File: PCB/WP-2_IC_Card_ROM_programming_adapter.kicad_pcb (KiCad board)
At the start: 2 copper layers, 17.8 x 49.5 mm, 3 parts, among them J1 Conn_01x38_Male, J2 Conn_02x16_Counter_Clockwise

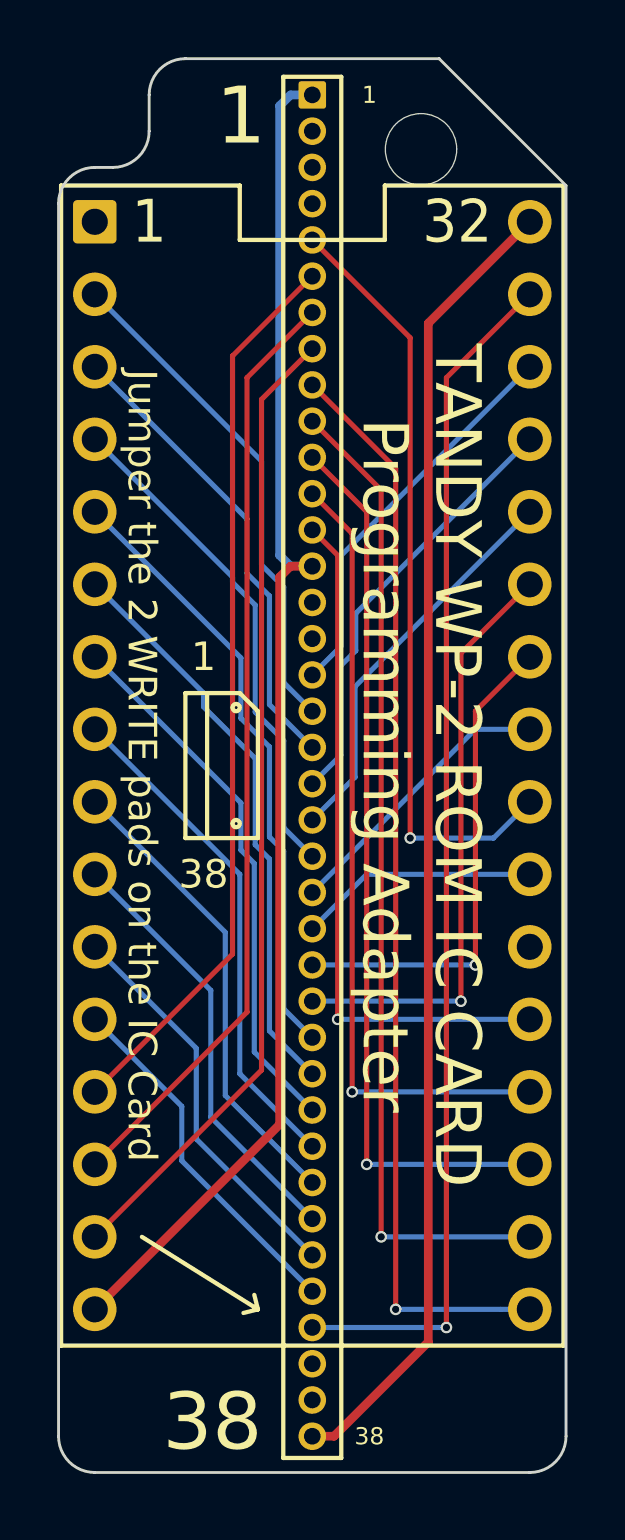
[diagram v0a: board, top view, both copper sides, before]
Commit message: fine-tune via-near-trace placements
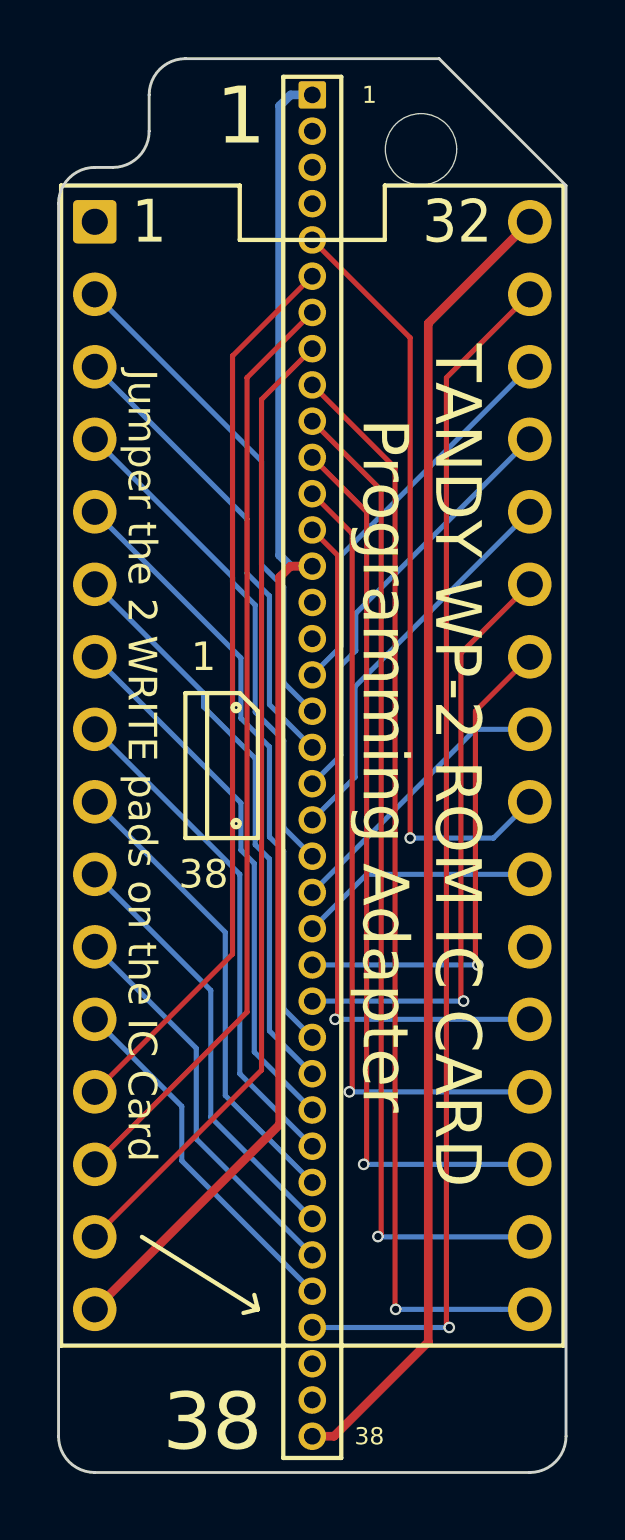
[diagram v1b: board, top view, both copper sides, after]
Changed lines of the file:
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@@
     (thickness 1.6)
     (drawings 58)
-    (tracks 133)
+    (tracks 141)
     (zones 0)
     (modules 3)
@@
       (effects (font (size 1 1) (thickness 0.15)))
     )
+    (fp_circle (center 0 0) (end 2.5 0) (layer Cmts.User) (width 0.15))
     (fp_circle (center 0 0) (end 2.75 0) (layer F.CrtYd) (width 0.05))
-    (fp_circle (center 0 0) (end 2.5 0) (layer Cmts.User) (width 0.15))
     (fp_text user %R (at 0.3 0) (layer F.Fab)
       (effects (font (size 1 1) (thickness 0.15)))
@@
   (segment (start 146.29 118.745) (end 147.306 118.745) (width 0.18) (layer B.Cu) (net 6))
   (segment (start 142.607 118.745) (end 146.29 118.745) (width 0.18) (layer B.Cu) (net 6))
-  (segment (start 142.607 89.281) (end 139.686 86.36) (width 0.18) (layer F.Cu) (net 6))
-  (segment (start 142.607 118.745) (end 142.607 89.281) (width 0.18) (layer F.Cu) (net 6))
-  (segment (start 142.099 116.205) (end 147.306 116.205) (width 0.18) (layer B.Cu) (net 7))
-  (via (at 142.099 116.205) (size 0.4064) (drill 0.254) (layers F.Cu B.Cu) (net 7))
+  (segment (start 142.586 89.26) (end 139.686 86.36) (width 0.18) (layer F.Cu) (net 6))
+  (segment (start 142.586 118.724) (end 142.586 89.26) (width 0.18) (layer F.Cu) (net 6))
+  (segment (start 142.607 118.745) (end 142.586 118.724) (width 0.18) (layer F.Cu) (net 6))
   (segment (start 142.099 90.043) (end 139.686 87.63) (width 0.18) (layer F.Cu) (net 7))
-  (segment (start 142.099 116.205) (end 142.099 90.043) (width 0.18) (layer F.Cu) (net 7))
-  (segment (start 141.591 113.665) (end 147.306 113.665) (width 0.18) (layer B.Cu) (net 8))
-  (via (at 141.591 113.665) (size 0.4064) (drill 0.254) (layers F.Cu B.Cu) (net 8))
+  (segment (start 141.986 116.195) (end 142.099 116.082) (width 0.18) (layer F.Cu) (net 7))
+  (segment (start 141.996 116.205) (end 147.306 116.205) (width 0.18) (layer B.Cu) (net 7))
+  (segment (start 141.986 116.195) (end 141.996 116.205) (width 0.18) (layer B.Cu) (net 7))
+  (segment (start 142.099 116.082) (end 142.099 90.043) (width 0.18) (layer F.Cu) (net 7))
+  (via (at 141.986 116.195) (size 0.4064) (drill 0.254) (layers F.Cu B.Cu) (net 7))
   (segment (start 141.591 90.805) (end 139.686 88.9) (width 0.18) (layer F.Cu) (net 8))
-  (segment (start 141.591 113.665) (end 141.591 90.805) (width 0.18) (layer F.Cu) (net 8))
-  (segment (start 141.083 111.125) (end 147.306 111.125) (width 0.18) (layer B.Cu) (net 9))
-  (via (at 141.083 111.125) (size 0.4064) (drill 0.254) (layers F.Cu B.Cu) (net 9))
+  (segment (start 141.591 113.56) (end 141.591 90.805) (width 0.18) (layer F.Cu) (net 8))
+  (segment (start 141.486 113.665) (end 141.591 113.56) (width 0.18) (layer F.Cu) (net 8))
+  (segment (start 141.486 113.665) (end 147.306 113.665) (width 0.18) (layer B.Cu) (net 8))
+  (via (at 141.486 113.665) (size 0.4064) (drill 0.254) (layers F.Cu B.Cu) (net 8))
   (segment (start 141.083 91.567) (end 139.686 90.17) (width 0.18) (layer F.Cu) (net 9))
-  (segment (start 141.083 111.125) (end 141.083 91.567) (width 0.18) (layer F.Cu) (net 9))
-  (via (at 140.575 108.585) (size 0.4064) (drill 0.254) (layers F.Cu B.Cu) (net 10))
-  (segment (start 140.575 108.585) (end 147.306 108.585) (width 0.18) (layer B.Cu) (net 10))
+  (segment (start 141.083 111.028) (end 141.083 91.567) (width 0.18) (layer F.Cu) (net 9))
+  (segment (start 140.986 111.125) (end 141.083 111.028) (width 0.18) (layer F.Cu) (net 9))
+  (segment (start 140.986 111.125) (end 147.306 111.125) (width 0.18) (layer B.Cu) (net 9))
+  (via (at 140.986 111.125) (size 0.4064) (drill 0.254) (layers F.Cu B.Cu) (net 9))
   (segment (start 140.575 92.329) (end 139.686 91.44) (width 0.18) (layer F.Cu) (net 10))
-  (segment (start 140.575 108.585) (end 140.575 92.329) (width 0.18) (layer F.Cu) (net 10))
+  (segment (start 140.575 108.496) (end 140.575 92.329) (width 0.18) (layer F.Cu) (net 10))
+  (segment (start 140.486 108.585) (end 140.575 108.496) (width 0.18) (layer F.Cu) (net 10))
+  (segment (start 140.486 108.585) (end 147.306 108.585) (width 0.18) (layer B.Cu) (net 10))
+  (via (at 140.486 108.585) (size 0.4064) (drill 0.254) (layers F.Cu B.Cu) (net 10))
   (segment (start 147.256 85.725) (end 147.306 85.725) (width 0.2032) (layer B.Cu) (net 11))
   (segment (start 147.226 85.695) (end 147.256 85.725) (width 0.2032) (layer B.Cu) (net 11))
@@
   (segment (start 139.686 105.41) (end 141.591 103.505) (width 0.18) (layer B.Cu) (net 18))
   (segment (start 145.401 97.79) (end 147.306 95.885) (width 0.18) (layer F.Cu) (net 19))
-  (segment (start 145.401 106.68) (end 145.401 97.79) (width 0.18) (layer F.Cu) (net 19))
-  (segment (start 145.401 106.68) (end 139.686 106.68) (width 0.18) (layer B.Cu) (net 19))
-  (via (at 145.401 106.68) (size 0.4064) (drill 0.254) (layers F.Cu B.Cu) (net 19))
+  (segment (start 145.401 106.595) (end 145.401 97.79) (width 0.18) (layer F.Cu) (net 19))
+  (segment (start 145.486 106.68) (end 145.401 106.595) (width 0.18) (layer F.Cu) (net 19))
+  (segment (start 145.486 106.68) (end 139.686 106.68) (width 0.18) (layer B.Cu) (net 19))
+  (via (at 145.486 106.68) (size 0.4064) (drill 0.254) (layers F.Cu B.Cu) (net 19))
   (segment (start 139.691 107.945) (end 139.686 107.95) (width 0.2032) (layer B.Cu) (net 20))
-  (segment (start 144.893 107.95) (end 144.893 95.758) (width 0.18) (layer F.Cu) (net 20))
-  (segment (start 144.888 107.945) (end 139.691 107.945) (width 0.18) (layer B.Cu) (net 20))
-  (segment (start 144.893 107.95) (end 144.888 107.945) (width 0.18) (layer B.Cu) (net 20))
   (segment (start 144.893 95.758) (end 147.306 93.345) (width 0.18) (layer F.Cu) (net 20))
-  (via (at 144.893 107.95) (size 0.4064) (drill 0.254) (layers F.Cu B.Cu) (net 20))
+  (segment (start 144.893 107.852) (end 144.893 95.758) (width 0.18) (layer F.Cu) (net 20))
+  (segment (start 144.986 107.945) (end 144.893 107.852) (width 0.18) (layer F.Cu) (net 20))
+  (segment (start 144.986 107.945) (end 139.691 107.945) (width 0.18) (layer B.Cu) (net 20))
+  (via (at 144.986 107.945) (size 0.4064) (drill 0.254) (layers F.Cu B.Cu) (net 20))
   (segment (start 138.686 108.22) (end 139.686 109.22) (width 0.18) (layer B.Cu) (net 21))
   (segment (start 138.686 102.695) (end 138.686 108.22) (width 0.18) (layer B.Cu) (net 21))
@@
   (segment (start 135.114 111.633) (end 135.114 113.538) (width 0.18) (layer B.Cu) (net 28))
   (segment (start 132.066 108.585) (end 135.114 111.633) (width 0.18) (layer B.Cu) (net 28))
+  (segment (start 144.486 119.38) (end 139.686 119.38) (width 0.18) (layer B.Cu) (net 29))
   (segment (start 144.385 86.106) (end 147.306 83.185) (width 0.18) (layer F.Cu) (net 29))
-  (segment (start 144.385 119.38) (end 139.686 119.38) (width 0.18) (layer B.Cu) (net 29))
-  (segment (start 144.385 119.38) (end 144.385 86.106) (width 0.18) (layer F.Cu) (net 29))
-  (via (at 144.385 119.38) (size 0.4064) (drill 0.254) (layers F.Cu B.Cu) (net 29))
+  (segment (start 144.385 119.279) (end 144.385 86.106) (width 0.18) (layer F.Cu) (net 29))
+  (segment (start 144.486 119.38) (end 144.385 119.279) (width 0.18) (layer F.Cu) (net 29))
+  (via (at 144.486 119.38) (size 0.4064) (drill 0.254) (layers F.Cu B.Cu) (net 29))
   (segment (start 140.448 123.19) (end 139.686 123.19) (width 0.3048) (layer F.Cu) (net 30))
   (segment (start 143.75 119.888) (end 140.448 123.19) (width 0.3048) (layer F.Cu) (net 30))

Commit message: increase via sizes and min soldermask width for PCBWAY
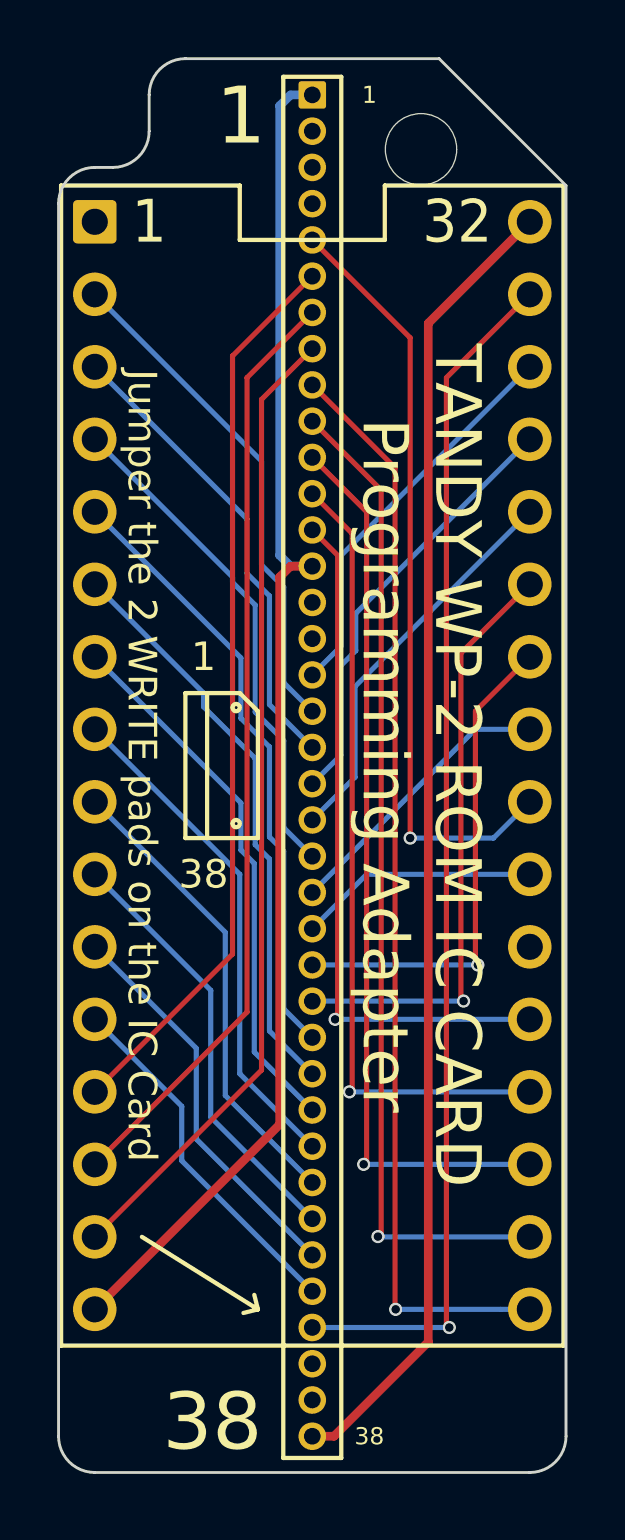
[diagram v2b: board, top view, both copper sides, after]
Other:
- board text added: "CENTER PINS OTHER SIDE"
- board text removed: "BOTTOM"
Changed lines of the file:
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@@
     (via_min_size 0.4)
     (via_min_drill 0.25)
-    (user_via 0.4064 0.254)
+    (user_via 0.46 0.3)
     (uvia_size 0.41)
     (uvia_drill 0.25)
@@
       (drillshape 0)
       (scaleselection 1)
-      (outputdirectory "GERBER_WP-2_IC_CARD_v003_ROM_programming_adapter"))
+      (outputdirectory "GERBER_WP-2_IC_CARD_ROM_programming_adapter"))
   )
   (net 0 "")
@@
     (pad 1 np_thru_hole circle (at 0 0) (size 2.5 2.5) (drill 2.5) (layers *.Cu *.Mask))
   )
+  (gr_text "CENTER PINS OTHER SIDE" (at 138.186 99.695 90) (layer B.SilkS)
+    (effects (font (size 1 1) (thickness 0.15)) (justify mirror))
+  )
   (gr_text "WP-2_IC_Card_ROM_programming_adapter v001" (at 143.186 99.695 90) (layer B.SilkS)
-    (effects (font (size 0.8 0.8) (thickness 0.08)) (justify mirror))
+    (effects (font (size 1 1) (thickness 0.1)) (justify mirror))
   )
   (gr_line (start 148.576 79.375) (end 144.131 74.93) (layer Edge.Cuts) (width 0.1))
@@
   (gr_text 1 (at 141.686 76.2) (layer F.SilkS)
     (effects (font (size 0.6 0.6) (thickness 0.1)))
-  )
-  (gr_text BOTTOM (at 134.86 99.695 90) (layer B.SilkS)
-    (effects (font (size 1 1) (thickness 0.15)) (justify mirror))
   )
   (gr_line (start 138.67 75.565) (end 140.702 75.565) (layer F.SilkS) (width 0.15))
@@
   )
   (gr_text github.com/bkw777/WP-2_IC_Card (at 144.766 99.695 90) (layer B.SilkS)
-    (effects (font (size 1 1) (thickness 0.15)) (justify mirror))
+    (effects (font (size 1 1) (thickness 0.1)) (justify mirror))
   )
   (gr_text "TANDY WP-2 ROM IC CARD" (at 144.766 99.695 -90) (layer F.SilkS)
@@
     (effects (font (size 1.6 1.6) (thickness 0.2)))
   )
-  (gr_text "DIP PINS THIS SIDE" (at 137.019 99.695 90) (layer B.SilkS)
+  (gr_text "DIP PINS THIS SIDE" (at 134.186 99.695 90) (layer B.SilkS)
     (effects (font (size 1 1) (thickness 0.15)) (justify mirror))
   )
@@
   (segment (start 138.924 92.71) (end 138.543 93.091) (width 0.3048) (layer F.Cu) (net 1))
   (segment (start 139.686 92.71) (end 138.924 92.71) (width 0.3048) (layer F.Cu) (net 1))
-  (via (at 143.115 102.235) (size 0.4064) (drill 0.254) (layers F.Cu B.Cu) (net 2))
+  (via (at 143.115 102.235) (size 0.46) (drill 0.3) (layers F.Cu B.Cu) (net 2))
   (segment (start 146.036 102.235) (end 147.306 100.965) (width 0.18) (layer B.Cu) (net 2))
   (segment (start 143.115 102.235) (end 146.036 102.235) (width 0.18) (layer B.Cu) (net 2))
@@
   (segment (start 137.908 110.363) (end 137.908 86.868) (width 0.18) (layer F.Cu) (net 5))
   (segment (start 132.066 116.205) (end 137.908 110.363) (width 0.18) (layer F.Cu) (net 5))
-  (via (at 142.607 118.745) (size 0.4064) (drill 0.254) (layers F.Cu B.Cu) (net 6))
+  (via (at 142.607 118.745) (size 0.46) (drill 0.3) (layers F.Cu B.Cu) (net 6))
   (segment (start 146.29 118.745) (end 147.306 118.745) (width 0.18) (layer B.Cu) (net 6))
   (segment (start 142.607 118.745) (end 146.29 118.745) (width 0.18) (layer B.Cu) (net 6))
@@
   (segment (start 141.986 116.195) (end 141.996 116.205) (width 0.18) (layer B.Cu) (net 7))
   (segment (start 142.099 116.082) (end 142.099 90.043) (width 0.18) (layer F.Cu) (net 7))
-  (via (at 141.986 116.195) (size 0.4064) (drill 0.254) (layers F.Cu B.Cu) (net 7))
+  (via (at 141.986 116.195) (size 0.46) (drill 0.3) (layers F.Cu B.Cu) (net 7))
   (segment (start 141.591 90.805) (end 139.686 88.9) (width 0.18) (layer F.Cu) (net 8))
   (segment (start 141.591 113.56) (end 141.591 90.805) (width 0.18) (layer F.Cu) (net 8))
   (segment (start 141.486 113.665) (end 141.591 113.56) (width 0.18) (layer F.Cu) (net 8))
   (segment (start 141.486 113.665) (end 147.306 113.665) (width 0.18) (layer B.Cu) (net 8))
-  (via (at 141.486 113.665) (size 0.4064) (drill 0.254) (layers F.Cu B.Cu) (net 8))
+  (via (at 141.486 113.665) (size 0.46) (drill 0.3) (layers F.Cu B.Cu) (net 8))
   (segment (start 141.083 91.567) (end 139.686 90.17) (width 0.18) (layer F.Cu) (net 9))
   (segment (start 141.083 111.028) (end 141.083 91.567) (width 0.18) (layer F.Cu) (net 9))
   (segment (start 140.986 111.125) (end 141.083 111.028) (width 0.18) (layer F.Cu) (net 9))
   (segment (start 140.986 111.125) (end 147.306 111.125) (width 0.18) (layer B.Cu) (net 9))
-  (via (at 140.986 111.125) (size 0.4064) (drill 0.254) (layers F.Cu B.Cu) (net 9))
+  (via (at 140.986 111.125) (size 0.46) (drill 0.3) (layers F.Cu B.Cu) (net 9))
   (segment (start 140.575 92.329) (end 139.686 91.44) (width 0.18) (layer F.Cu) (net 10))
   (segment (start 140.575 108.496) (end 140.575 92.329) (width 0.18) (layer F.Cu) (net 10))
   (segment (start 140.486 108.585) (end 140.575 108.496) (width 0.18) (layer F.Cu) (net 10))
   (segment (start 140.486 108.585) (end 147.306 108.585) (width 0.18) (layer B.Cu) (net 10))
-  (via (at 140.486 108.585) (size 0.4064) (drill 0.254) (layers F.Cu B.Cu) (net 10))
+  (via (at 140.486 108.585) (size 0.46) (drill 0.3) (layers F.Cu B.Cu) (net 10))
   (segment (start 147.256 85.725) (end 147.306 85.725) (width 0.2032) (layer B.Cu) (net 11))
   (segment (start 147.226 85.695) (end 147.256 85.725) (width 0.2032) (layer B.Cu) (net 11))
@@
   (segment (start 145.486 106.68) (end 145.401 106.595) (width 0.18) (layer F.Cu) (net 19))
   (segment (start 145.486 106.68) (end 139.686 106.68) (width 0.18) (layer B.Cu) (net 19))
-  (via (at 145.486 106.68) (size 0.4064) (drill 0.254) (layers F.Cu B.Cu) (net 19))
+  (via (at 145.486 106.68) (size 0.46) (drill 0.3) (layers F.Cu B.Cu) (net 19))
   (segment (start 139.691 107.945) (end 139.686 107.95) (width 0.2032) (layer B.Cu) (net 20))
   (segment (start 144.893 95.758) (end 147.306 93.345) (width 0.18) (layer F.Cu) (net 20))
@@
   (segment (start 144.986 107.945) (end 144.893 107.852) (width 0.18) (layer F.Cu) (net 20))
   (segment (start 144.986 107.945) (end 139.691 107.945) (width 0.18) (layer B.Cu) (net 20))
-  (via (at 144.986 107.945) (size 0.4064) (drill 0.254) (layers F.Cu B.Cu) (net 20))
+  (via (at 144.986 107.945) (size 0.46) (drill 0.3) (layers F.Cu B.Cu) (net 20))
   (segment (start 138.686 108.22) (end 139.686 109.22) (width 0.18) (layer B.Cu) (net 21))
   (segment (start 138.686 102.695) (end 138.686 108.22) (width 0.18) (layer B.Cu) (net 21))
@@
   (segment (start 144.385 119.279) (end 144.385 86.106) (width 0.18) (layer F.Cu) (net 29))
   (segment (start 144.486 119.38) (end 144.385 119.279) (width 0.18) (layer F.Cu) (net 29))
-  (via (at 144.486 119.38) (size 0.4064) (drill 0.254) (layers F.Cu B.Cu) (net 29))
+  (via (at 144.486 119.38) (size 0.46) (drill 0.3) (layers F.Cu B.Cu) (net 29))
   (segment (start 140.448 123.19) (end 139.686 123.19) (width 0.3048) (layer F.Cu) (net 30))
   (segment (start 143.75 119.888) (end 140.448 123.19) (width 0.3048) (layer F.Cu) (net 30))
